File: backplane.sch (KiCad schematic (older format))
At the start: 29 parts, among them J100 SEPERATION_SW, J105 +X SOLAR PANEL, J106 -X SOLAR PANEL, J107 +Y SOLAR PANEL, J200_1 HSEC8-160-01-S-DV-A-K-TR, J200_2 HSEC8-160-01-S-DV-A-K-TR, J200_3 HSEC8-160-01-S-DV-A-K-TR, J200_4 HSEC8-160-01-S-DV-A-K-TR, J200_5 HSEC8-160-01-S-DV-A-K-TR, J200_6 HSEC8-160-01-S-DV-A-K-TR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

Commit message: final changes before ordering
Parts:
- added J101: BURN_WIRES, CubeSat_Backplane:DF13-4P-1.25(75), symbol Connector_Generic:Conn_01x05
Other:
- note added: "Burn Wire Connectors"
- note added: "burn1"
- note added: "burn2"
- note added: "may need to move these in future"
- note removed: "Breakout Connectors"
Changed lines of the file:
@@
 Text Notes 13150 13900 0    100  ~ 0
 CHS, GND Jumper
-Text Notes 18150 4500 0    100  ~ 20
-Breakout Connectors
+Text Notes 17350 3450 0    100  ~ 20
+Burn Wire Connectors
 $Comp
 L Connector_Generic:Conn_02x30_Odd_Even J301
@@
 Text Notes 17400 15500 0    100  ~ 20
 BACKPLANE
+$Comp
+L Connector_Generic:Conn_01x05 J101
+U 1 1 61E229FD
+P 17600 3950
+F 0 "J101" H 17518 4357 50  0000 C CNN
+F 1 "BURN_WIRES" H 17518 4266 50  0000 C CNN
+F 2 "CubeSat_Backplane:DF13-4P-1.25(75)" H 17600 3950 50  0001 C CNN
+F 3 "F13-4P-1.25(76)" H 17518 4175 50  0000 C CNN
+	1    17600 3950
+	-1   0    0    -1
+$EndComp
+Text Label 17800 4050 0    60   ~ 0
+GND
+Text Label 17800 3850 0    60   ~ 0
+GND
+Text Label 17800 3750 0    60   ~ 0
+H1-1
+Text Label 17800 3950 0    60   ~ 0
+H1-2
+Text Notes 18150 3850 0    100  ~ 0
+burn1
+Text Notes 18150 4050 0    100  ~ 0
+burn2
+Text Notes 18700 3950 0    100  ~ 0
+may need to move these in future
+Text Label 17800 4150 0    60   ~ 0
+CHS
 $EndSCHEMATC

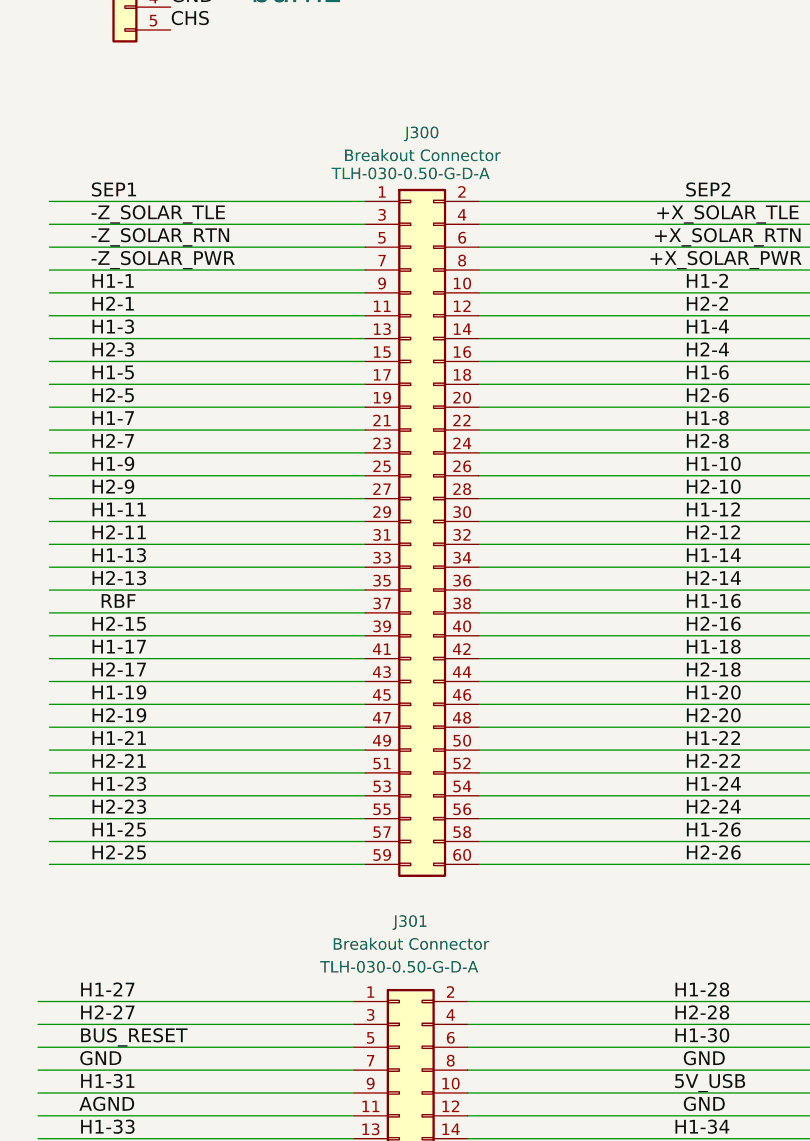
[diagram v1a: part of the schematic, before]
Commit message: changed breakout connector
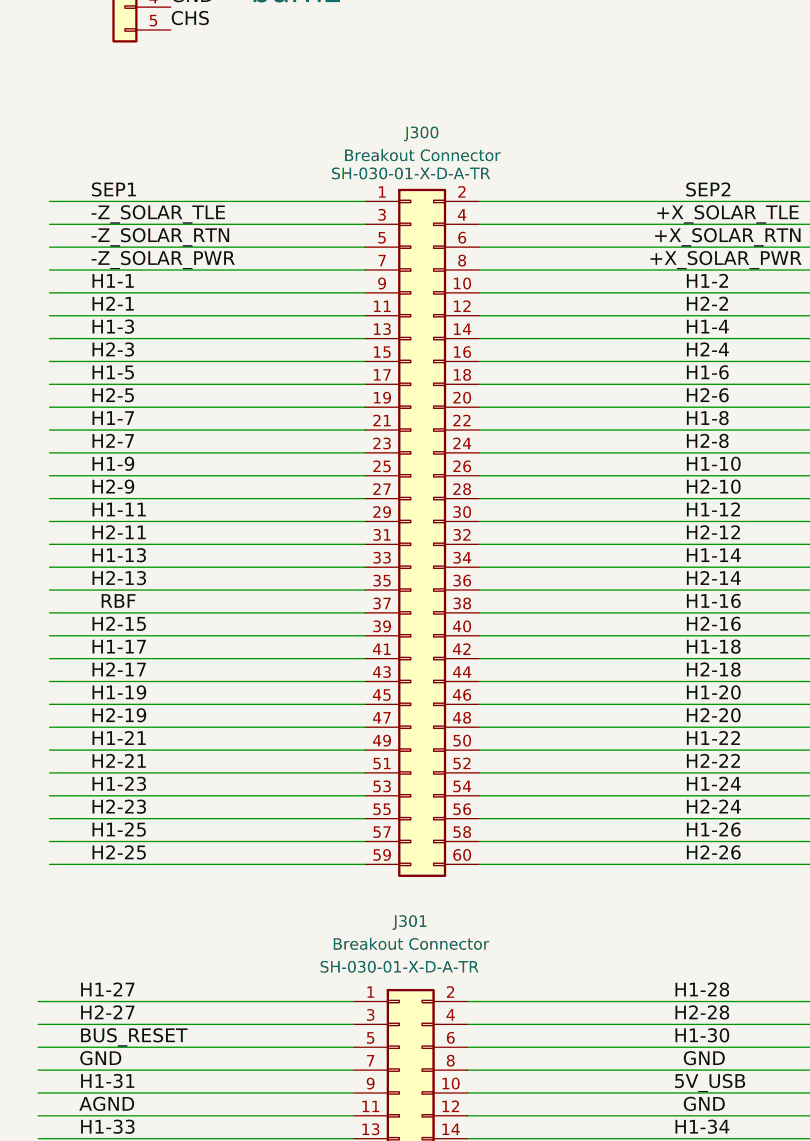
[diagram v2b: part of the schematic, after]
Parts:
- J300, J301: footprint CubeSat_Backplane:TLH-030-0.50-G-D-A -> CubeSat_Backplane:SAMTEC_LSH-030-01-X-D-A-TR; Manufacturer Part Number 1 TLH-030-0.50-G-D-A -> SH-030-01-X-D-A-TR
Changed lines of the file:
@@
 F 0 "J301" H 18850 11550 50  0000 C CNN
 F 1 "Breakout Connector" H 18850 11450 50  0000 C CNN
-F 2 "CubeSat_Backplane:TLH-030-0.50-G-D-A" H 18800 9800 50  0001 C CNN
-F 3 "TLH-030-0.50-G-D-A" H 18800 11350 50  0000 C CNN
-F 4 "TLH-030-0.50-G-D-A" H 18800 9800 50  0001 C CNN "Manufacturer Part Number 1"
+F 2 "CubeSat_Backplane:SAMTEC_LSH-030-01-X-D-A-TR" H 18800 9800 50  0001 C CNN
+F 3 "SH-030-01-X-D-A-TR" H 18800 11350 50  0000 C CNN
+F 4 "SH-030-01-X-D-A-TR" H 18800 9800 50  0001 C CNN "Manufacturer Part Number 1"
 	1    18800 9800
-	1    0    0    -1
-$EndComp
-$Comp
-L Connector_Generic:Conn_02x30_Odd_Even J300
-U 1 1 A5767F5B
-P 18850 6300
-F 0 "J300" H 18900 8000 50  0000 C CNN
-F 1 "Breakout Connector" H 18900 7900 50  0000 C CNN
-F 2 "CubeSat_Backplane:TLH-030-0.50-G-D-A" H 18850 6300 50  0001 C CNN
-F 3 "TLH-030-0.50-G-D-A" H 18850 7850 50  0000 C TNN
-F 4 "TLH-030-0.50-G-D-A" H 18850 6300 50  0001 C CNN "Manufacturer Part Number 1"
-	1    18850 6300
 	1    0    0    -1
 $EndComp
@@
 Wire Wire Line
 	20640 11300 19100 11300
-Wire Wire Line
-	18650 4900 17270 4900
-Wire Wire Line
-	18650 5000 17270 5000
-Wire Wire Line
-	18650 5100 17270 5100
-Wire Wire Line
-	18650 5200 17270 5200
-Wire Wire Line
-	18650 5300 17270 5300
-Wire Wire Line
-	18650 5400 17270 5400
-Wire Wire Line
-	18650 5500 17270 5500
-Wire Wire Line
-	18650 5600 17270 5600
-Wire Wire Line
-	18650 5700 17270 5700
-Wire Wire Line
-	18650 5800 17270 5800
-Wire Wire Line
-	18650 5900 17270 5900
-Wire Wire Line
-	18650 6000 17270 6000
-Wire Wire Line
-	18650 6100 17270 6100
-Wire Wire Line
-	18650 6200 17270 6200
-Wire Wire Line
-	18650 6300 17270 6300
-Wire Wire Line
-	18650 6400 17270 6400
-Wire Wire Line
-	18650 6500 17270 6500
-Wire Wire Line
-	18650 6600 17270 6600
-Wire Wire Line
-	18650 6700 17270 6700
-Wire Wire Line
-	18650 6800 17270 6800
-Wire Wire Line
-	18650 6900 17270 6900
-Wire Wire Line
-	18650 7000 17270 7000
-Wire Wire Line
-	18650 7100 17270 7100
-Wire Wire Line
-	18650 7200 17270 7200
-Wire Wire Line
-	18650 7300 17270 7300
-Wire Wire Line
-	18650 7400 17270 7400
-Wire Wire Line
-	18650 7500 17270 7500
-Wire Wire Line
-	18650 7600 17270 7600
-Wire Wire Line
-	18650 7700 17270 7700
-Wire Wire Line
-	18650 7800 17270 7800
 Wire Wire Line
 	18600 8400 17220 8400
@@
 Text Label 17800 4150 0    60   ~ 0
 CHS
+Wire Wire Line
+	18650 7800 17270 7800
+Wire Wire Line
+	18650 7700 17270 7700
+Wire Wire Line
+	18650 7600 17270 7600
+Wire Wire Line
+	18650 7500 17270 7500
+Wire Wire Line
+	18650 7400 17270 7400
+Wire Wire Line
+	18650 7300 17270 7300
+Wire Wire Line
+	18650 7200 17270 7200
+Wire Wire Line
+	18650 7100 17270 7100
+Wire Wire Line
+	18650 7000 17270 7000
+Wire Wire Line
+	18650 6900 17270 6900
+Wire Wire Line
+	18650 6800 17270 6800
+Wire Wire Line
+	18650 6700 17270 6700
+Wire Wire Line
+	18650 6600 17270 6600
+Wire Wire Line
+	18650 6500 17270 6500
+Wire Wire Line
+	18650 6400 17270 6400
+Wire Wire Line
+	18650 6300 17270 6300
+Wire Wire Line
+	18650 6200 17270 6200
+Wire Wire Line
+	18650 6100 17270 6100
+Wire Wire Line
+	18650 6000 17270 6000
+Wire Wire Line
+	18650 5900 17270 5900
+Wire Wire Line
+	18650 5800 17270 5800
+Wire Wire Line
+	18650 5700 17270 5700
+Wire Wire Line
+	18650 5600 17270 5600
+Wire Wire Line
+	18650 5500 17270 5500
+Wire Wire Line
+	18650 5400 17270 5400
+Wire Wire Line
+	18650 5300 17270 5300
+Wire Wire Line
+	18650 5200 17270 5200
+Wire Wire Line
+	18650 5100 17270 5100
+Wire Wire Line
+	18650 5000 17270 5000
+Wire Wire Line
+	18650 4900 17270 4900
+$Comp
+L Connector_Generic:Conn_02x30_Odd_Even J300
+U 1 1 A5767F5B
+P 18850 6300
+F 0 "J300" H 18900 8000 50  0000 C CNN
+F 1 "Breakout Connector" H 18900 7900 50  0000 C CNN
+F 2 "CubeSat_Backplane:SAMTEC_LSH-030-01-X-D-A-TR" H 18850 6300 50  0001 C CNN
+F 3 "SH-030-01-X-D-A-TR" H 18850 7850 50  0000 C TNN
+F 4 "SH-030-01-X-D-A-TR" H 18850 6300 50  0001 C CNN "Manufacturer Part Number 1"
+	1    18850 6300
+	1    0    0    -1
+$EndComp
 $EndSCHEMATC

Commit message: backplane sepsw emulator board
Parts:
- J300, J301: Manufacturer Part Number 1 SH-030-01-X-D-A-TR -> LSH-030-01-X-D-A-TR
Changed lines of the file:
@@
 F 1 "Breakout Connector" H 18850 11450 50  0000 C CNN
 F 2 "CubeSat_Backplane:SAMTEC_LSH-030-01-X-D-A-TR" H 18800 9800 50  0001 C CNN
-F 3 "SH-030-01-X-D-A-TR" H 18800 11350 50  0000 C CNN
-F 4 "SH-030-01-X-D-A-TR" H 18800 9800 50  0001 C CNN "Manufacturer Part Number 1"
+F 3 "LSH-030-01-X-D-A-TR" H 18800 11350 50  0000 C CNN
+F 4 "LSH-030-01-X-D-A-TR" H 18800 9800 50  0001 C CNN "Manufacturer Part Number 1"
 	1    18800 9800
 	1    0    0    -1
@@
 F 1 "Breakout Connector" H 18900 7900 50  0000 C CNN
 F 2 "CubeSat_Backplane:SAMTEC_LSH-030-01-X-D-A-TR" H 18850 6300 50  0001 C CNN
-F 3 "SH-030-01-X-D-A-TR" H 18850 7850 50  0000 C TNN
-F 4 "SH-030-01-X-D-A-TR" H 18850 6300 50  0001 C CNN "Manufacturer Part Number 1"
+F 3 "LSH-030-01-X-D-A-TR" H 18850 7850 50  0000 C TNN
+F 4 "LSH-030-01-X-D-A-TR" H 18850 6300 50  0001 C CNN "Manufacturer Part Number 1"
 	1    18850 6300
 	1    0    0    -1

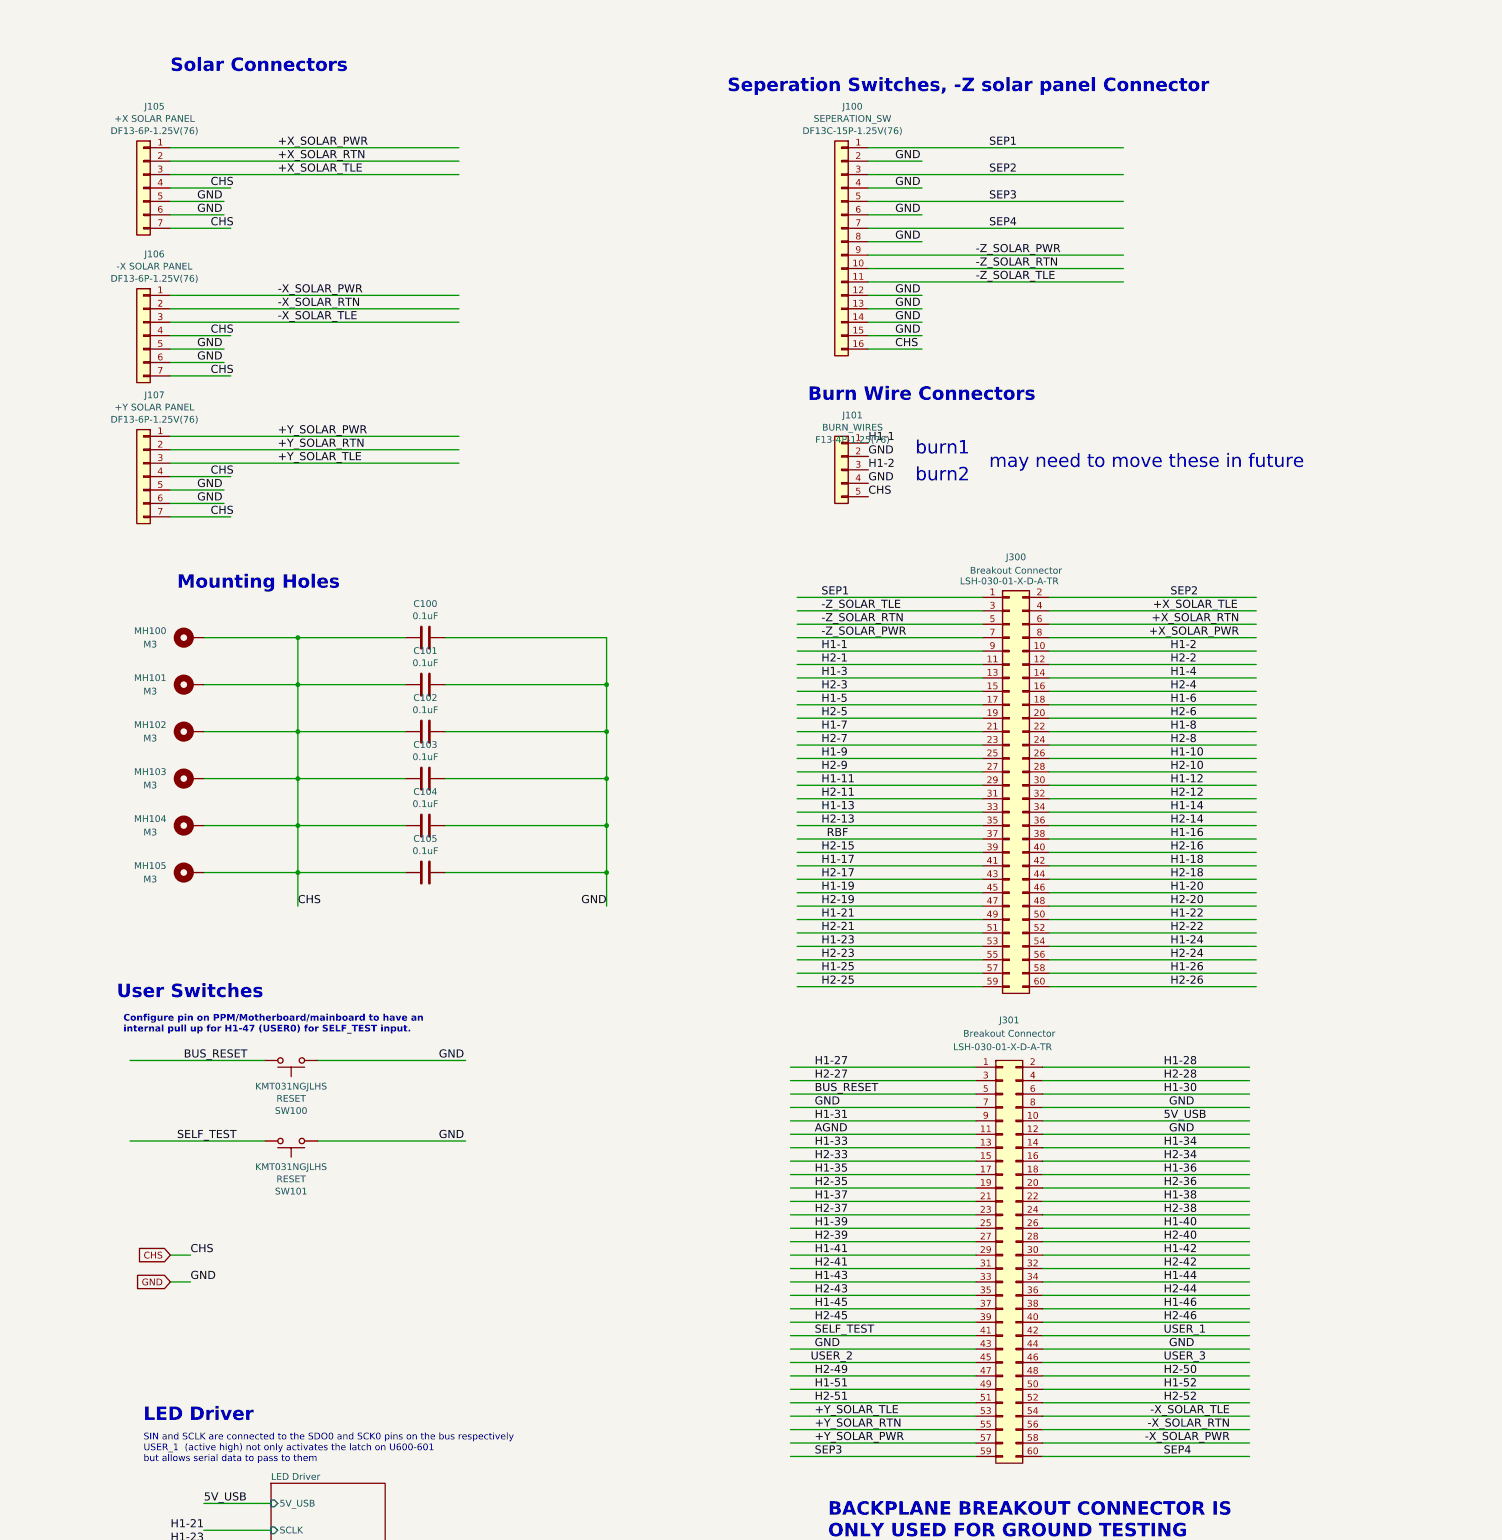
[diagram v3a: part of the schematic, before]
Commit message: changed to 2x30 1.27mm headers
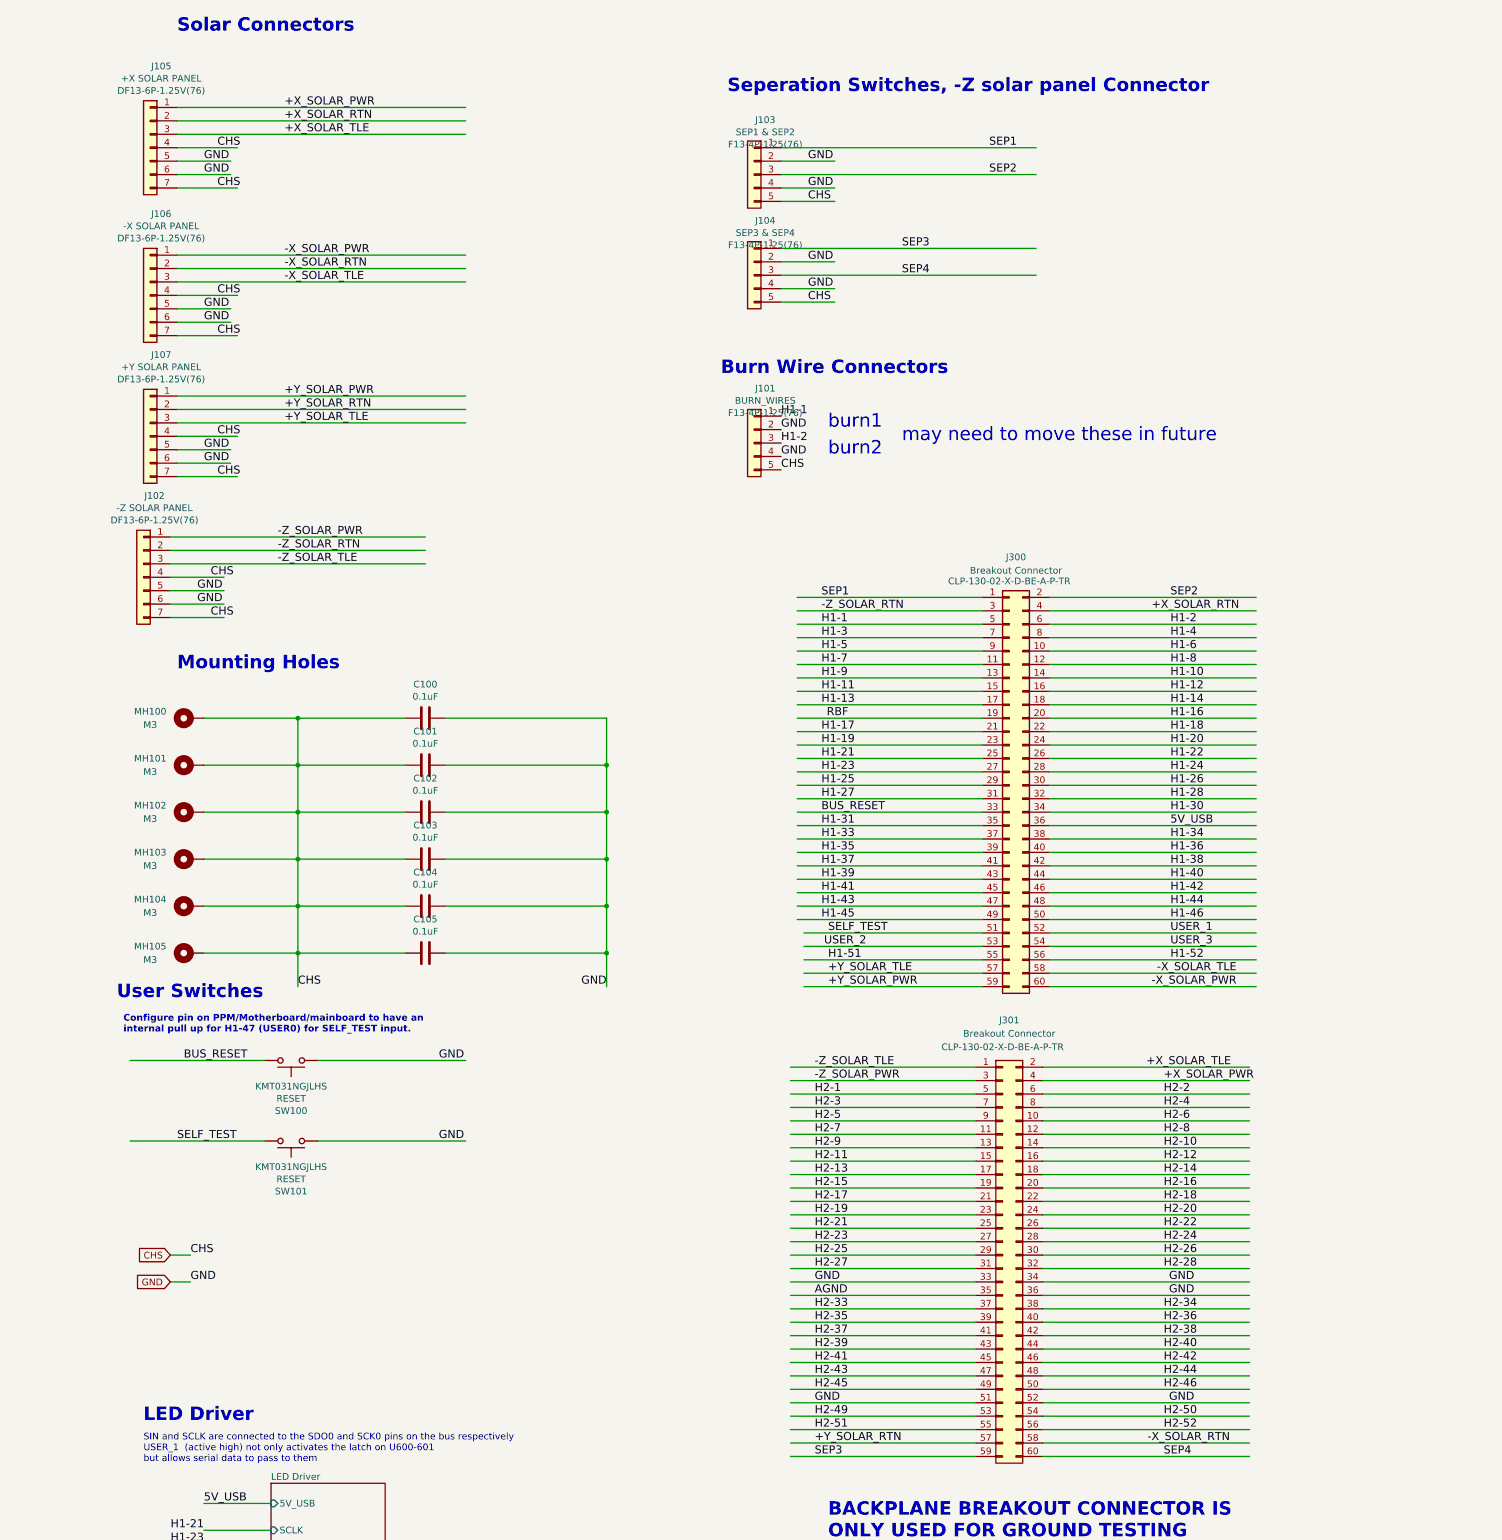
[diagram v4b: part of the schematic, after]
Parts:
- removed J100: SEPERATION_SW, CubeSat_Backplane:DF13-15P-1.25H(75), symbol Connector_Generic:Conn_01x16
- added J102: -Z SOLAR PANEL, CubeSat_Backplane:DF13-6P-1.25(75), symbol Connector_Generic:Conn_01x07
- added J103: SEP1 & SEP2, CubeSat_Backplane:DF13-4P-1.25(75), symbol Connector_Generic:Conn_01x05
- added J104: SEP3 & SEP4, CubeSat_Backplane:DF13-4P-1.25(75), symbol Connector_Generic:Conn_01x05
- J300, J301: footprint CubeSat_Backplane:SAMTEC_LSH-030-01-X-D-A-TR -> CubeSat_Backplane:SAMTEC_CLP-130-02-X-D-BE-A-P-TR; Manufacturer Part Number 1 LSH-030-01-X-D-A-TR -> CLP-130-02-X-D-BE-A-P-TR
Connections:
- wire segments 1161 -> 1162
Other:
- moved on the sheet: C100, C101, C102, C103, C104, C105, J101, J105, J106, J107, MH100, MH101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
